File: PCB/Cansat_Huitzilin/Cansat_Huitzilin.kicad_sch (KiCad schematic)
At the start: 0 parts

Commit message: Actualización de la PCB
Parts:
- added C1: 10uf, Capacitor_SMD:C_0603_1608Metric, symbol Device:C
- added C10, C11, C12, C9: 22uF, Capacitor_SMD:C_0603_1608Metric, symbol Device:C
- added C13, C14, C2: 10uF, Capacitor_SMD:C_0603_1608Metric, symbol Device:C
- added C15, C17, C18, C19, C20, C22, C23, C3, C5, C8: 100nF, Capacitor_SMD:C_0603_1608Metric, symbol Device:C
- added C16: 1uF, Capacitor_SMD:C_0603_1608Metric, symbol Device:C
- added C21: 2.2uF, Capacitor_SMD:C_0603_1608Metric, symbol Device:C
- added C25, C26: C_Polarized, Capacitor_SMD:CP_Elec_6.3x5.8, symbol Device:C_Polarized
- added C4, C7: 10nF, Capacitor_SMD:C_0603_1608Metric, symbol Device:C
- added C6: 2.7nF, Capacitor_SMD:C_0603_1608Metric, symbol Device:C
- added D1: D_Schottky, Diode_SMD:D_SOD-123F, symbol Device:D_Schottky
- added H1, H2, H3, H4: MountingHole_Pad, MountingHole:MountingHole_3.2mm_M3, symbol Mechanical:MountingHole_Pad
- added IC1: AP64501SP-13, Package_SO:SOIC-8-1EP_3.9x4.9mm_P1.27mm_EP2.29x3mm, symbol AP64501SP-13:AP64501SP-13
- added IC2: 114993390, 114993390, symbol SamacSys_Parts:114993390
- added IC3: BMM350, BGA9C40P3X3_128X128X54, symbol SamacSys_Parts:BMM350
- added IC4: BMI323, BMI323, symbol SamacSys_Parts:BMI323
- added IC5: STCC4-D-R3, STCC4DR3, symbol SamacSys_Parts:STCC4-D-R3
- added IC6: SHT40-AD1B-R2, SHT40AD1BR2, symbol SamacSys_Parts:SHT40-AD1B-R2
- added J1: Screw_Terminal_01x02, TerminalBlock:TerminalBlock_MaiXu_MX126-5.0-02P_1x02_P5.00mm, symbol Connector:Screw_Terminal_01x02
- added J2: Conn_01x04, Connector_PinHeader_2.54mm:PinHeader_1x04_P2.54mm_Vertical, symbol Connector_Generic:Conn_01x04
- added J3, J5: Conn_01x03, Connector_PinHeader_2.54mm:PinHeader_1x03_P2.54mm_Vertical, symbol Connector_Generic:Conn_01x03
- added J4: Conn_01x06, SM06BPASSTBTLFSN, symbol Connector_Generic:Conn_01x06
- added J6: 503398-1892, 5033981892, symbol SamacSys_Parts:503398-1892
- added L1: 3.3uH, Inductor_SMD:L_Wuerth_WE-PD-Typ-LS, symbol Device:L_Ferrite
- added L2: 10uH, Inductor_SMD:L_1210_3225Metric_Pad1.42x2.65mm_HandSolder, symbol Device:L_Ferrite
- added LS1: MLT-8530, MLT8530, symbol SamacSys_Parts:MLT-8530
- added PS1: LD39200DPUR, SON80P400X400X100-9N-D, symbol SamacSys_Parts:LD39200DPUR
- added Q1: NPN, Package_TO_SOT_SMD:SOT-23, symbol Simulation_SPICE:NPN
- added R1: 100k, Resistor_SMD:R_0603_1608Metric, symbol Device:R_US
- added R10, R12, R13, R14, R15, R16, R17, R5, R9: 10k, Resistor_SMD:R_0603_1608Metric, symbol Device:R_US
- added R11: 1k, Resistor_SMD:R_0603_1608Metric, symbol Device:R_US
- added R2: 15.8k, Resistor_SMD:R_0603_1608Metric, symbol Device:R_US
- added R3: 2.2k, Resistor_SMD:R_0603_1608Metric, symbol Device:R_US
- added R4: 8.87k, Resistor_SMD:R_0603_1608Metric, symbol Device:R_US
- added R6, R7: 4.7k, Resistor_SMD:R_0603_1608Metric, symbol Device:R_US
- added R8: 56k, Resistor_SMD:R_0603_1608Metric, symbol Device:R_US
- added S1, S2: PTS526SM15SMTR2_LFS, PTS526SM15SMTR2LFS, symbol SamacSys_Parts:PTS526SM15SMTR2_LFS
- added SW1: SW_Wuerth_450301014042, Button_Switch_THT:SW_Slide-03_Wuerth-WS-SLTV_10x2.5x6.4_P2.54mm, symbol Switch:SW_Wuerth_450301014042
- added TP1, TP2: TestPoint, TestPoint:TestPoint_Pad_D1.0mm, symbol Connector:TestPoint
- added U1: ESP32-S3-MINI-1U, RF_Module:ESP32-S2-MINI-1U, symbol RF_Module:ESP32-S3-MINI-1U
- added U3: BMP581, BMP581, symbol SamacSys_Parts:BMP581
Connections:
- new net: J6.8 (DAT1), R16.1
- new net: IC1.3 (EN), R1.2, TP1.1
- new net: C10.1, C11.1, C7.2, C8.1, C9.1, L1.2, L2.1, R4.1
- new net: PS1.3 (ADJ/SENSE), R8.1, R9.2
- new net: PS1.5 (PG), TP2.1
- new net: C4.1, IC1.4 (SS)
- new net: D1.2 (A), LS1.3 (-LEAD), Q1.1 (C)
- new net: C5.1, IC1.1 (BST)
- new net: C7.1, IC1.5 (FB), R3.2, R4.2
- new net: IC1.6 (COMP), R2.2
- new net: C5.2, IC1.8 (SW), L1.1
- new net: C6.1, R2.1
- new net: J6.1 (DAT2), R17.1
- new net: Q1.2 (B), R11.2
- new net: C21.1, IC3.C2 (CRST)
- new net: IC5.2 (SDA_C), IC6.1 (SDA)
- new net +3.3V: C14.1, C15.1, C17.1, C18.1, C19.1, C20.1, C22.2, C23.1, IC2.8 (VCC), IC3.B3 (VDDIO), IC3.C1 (VDD), IC4.12 (CSB), IC4.5 (VDDIO), IC4.8 (VDD), IC5.6 (VDDIO), IC5.7 (VDD), IC6.3 (VDD), J2.4 (Pin_4), J6.4 (VDD), PS1.1 (OUT_1), PS1.2 (OUT_2), R10.2, R12.1, R13.2, R14.2, R15.2, R16.2, R17.2, R5.2, R6.1, R7.1, R8.2, U1.3 (3V3), U3.1 (VDDIO), U3.10 (VDD), U3.6 (CSB)
- new net +4V: C12.1, C13.1, C25.1, C26.1, D1.1 (K), J3.2 (Pin_2), J4.3 (Pin_3), J5.2 (Pin_2), L2.2, LS1.2 (+LEAD), PS1.6 (EN), PS1.7 (IN_1), PS1.8 (IN_2)
- new net +9V: J1.1 (Pin_1), SW1.1 (B)
- new net BOOT: R12.2, S2.1 (COM_1), U1.4 (IO0)
- new net BUSY: IC2.11 (BUSY), U1.13 (IO9)
- new net BUZZER: R11.1, U1.38 (IO42)
- new net CS_SD: J6.2 (CD/DAT3), R10.1, U1.37 (IO41)
- new net DIO1: IC2.12 (DIO1), U1.18 (IO14)
- new net Enable ESP: C16.1, R5.1, S1.1 (COM_1), U1.45 (EN)
- new net GND: C1.2, C10.2, C11.2, C12.2, C13.2, C14.2, C15.2, C16.2, C17.2, C18.2, C19.2, C2.2, C20.2, C21.2, C22.1, C23.2, C25.2, C26.2, C3.2, C4.2, C6.2, C8.2, C9.2, H1.1, H2.1, H3.1, H4.1, IC1.7 (GND), IC1.9 (EP), IC2.10 (GND_2), IC2.7 (GND_1), IC3.B1 (GND), IC3.B2 (ADSEL), IC3.C3 (BYPASS), IC4.1 (SDO), IC4.6 (GNDIO), IC4.7 (GND), IC5.3 (ADDR), IC5.4 (VSS), IC6.4 (VSS), J1.2 (Pin_2), J2.1 (Pin_1), J3.1 (Pin_1), J4.4 (Pin_4), J5.1 (Pin_1), J6.11, J6.12, J6.13, J6.14, J6.6 (VSS), PS1.4 (GND_1), PS1.9 (GND_2), Q1.3 (E), R3.1, R9.1, S1.3 (NO_1), S2.3 (NO_1), U1.1 (GND), U1.2 (GND), U1.42 (GND), U1.43 (GND), U1.46 (GND), U1.47 (GND), U1.48 (GND), U1.49 (GND), U1.50 (GND), U1.51 (GND), U1.52 (GND), U1.53 (GND), U1.54 (GND), U1.55 (GND), U1.56 (GND), U1.57 (GND), U1.58 (GND), U1.59 (GND), U1.60 (GND), U1.61 (GND), U1.62 (GND), U1.63 (GND), U1.64 (GND), U1.65 (GND), U3.3 (VSS_1), U3.5 (SDO), U3.8 (VSS_2), U3.9 (VSS_3)
- new net MISO: IC2.2 (MISO), J6.7 (DAT0), R15.1, U1.17 (IO13)
- new net MOSI: IC2.3 (MOSI), J6.3 (CMD), R13.1, U1.15 (IO11)
- new net NRST: IC2.5 (NRST), U1.25 (IO21)
- new net NSS: IC2.6 (NSS), U1.14 (IO10)
- new net RF_SW: IC2.1 (RF_SW_), U1.36 (IO40)
- new net RX: J2.2 (Pin_2), U1.40 (RXD0)
- new net RX_GPS: J4.5 (Pin_5), U1.21 (IO17)
- new net SCK: IC2.4 (SCK), J6.5 (CLK), R14.1, U1.16 (IO12)
- new net SCL: IC3.A3 (SCK), IC4.13 (SCX), IC5.1 (SCL), R7.2, U1.6 (IO2), U3.2 (SCK)
- new net SCL_SHT4: IC5.8 (SCL_C), IC6.2 (SCL)
- new net SDA: IC3.A2 (SDA), IC4.14 (SDX), IC5.5 (SDA), R6.2, U1.5 (IO1), U3.4 (SDI)
- new net SERVO 1: J3.3 (Pin_3), U1.8 (IO4)
- new net SERVO 2: J5.3 (Pin_3), U1.9 (IO5)
- new net Sw_9v: C1.1, C2.1, C3.1, IC1.2 (VIN), R1.1, SW1.3 (A)
- new net TX: J2.3 (Pin_3), U1.39 (TXD0)
- new net TX_GPS: J4.6 (Pin_6), U1.22 (IO18)
- no-connect marks 0 -> 20
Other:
- note added: "BMI-323"
- note added: "BMP-581"
- note added: "Buzzer"
- note added: "COMUNICACION"
- note added: "Conector"
- note added: "DC-DC BUCK 4V OUT"
- note added: "Enable ESP32"
- note added: "GPS UART"
- note added: "I2C BUS"
- note added: "LECTOR SD"
- note added: "LIS2MDL"
- note added: "PROGRAMACION POR UART"
- note added: "Regulador Lineal 4v a 3.3v"
- note added: "SERVOS"
- note added: "STCC4"
- note added: "SWITCH 9V"
- company: (none) -> S.T.R.I.K.E.
- title: (none) -> Cansat

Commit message: Actualización del diseño PCB
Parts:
- added J7: Conn_01x04, Connector_PinHeader_2.54mm:PinHeader_1x04_P2.54mm_Vertical, symbol Connector_Generic:Conn_01x04
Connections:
- net +3.3V: now also J7.4 (Pin_4)
- net GND: now also J7.1 (Pin_1)
- net TX_PI: now reaches U1.27 (IO47)
- net TX_PI: now also J7.3 (Pin_3)
- net RX_PI: now reaches U1.30 (IO48)
- net RX_PI: now also J7.2 (Pin_2)
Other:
- note added: "pi"

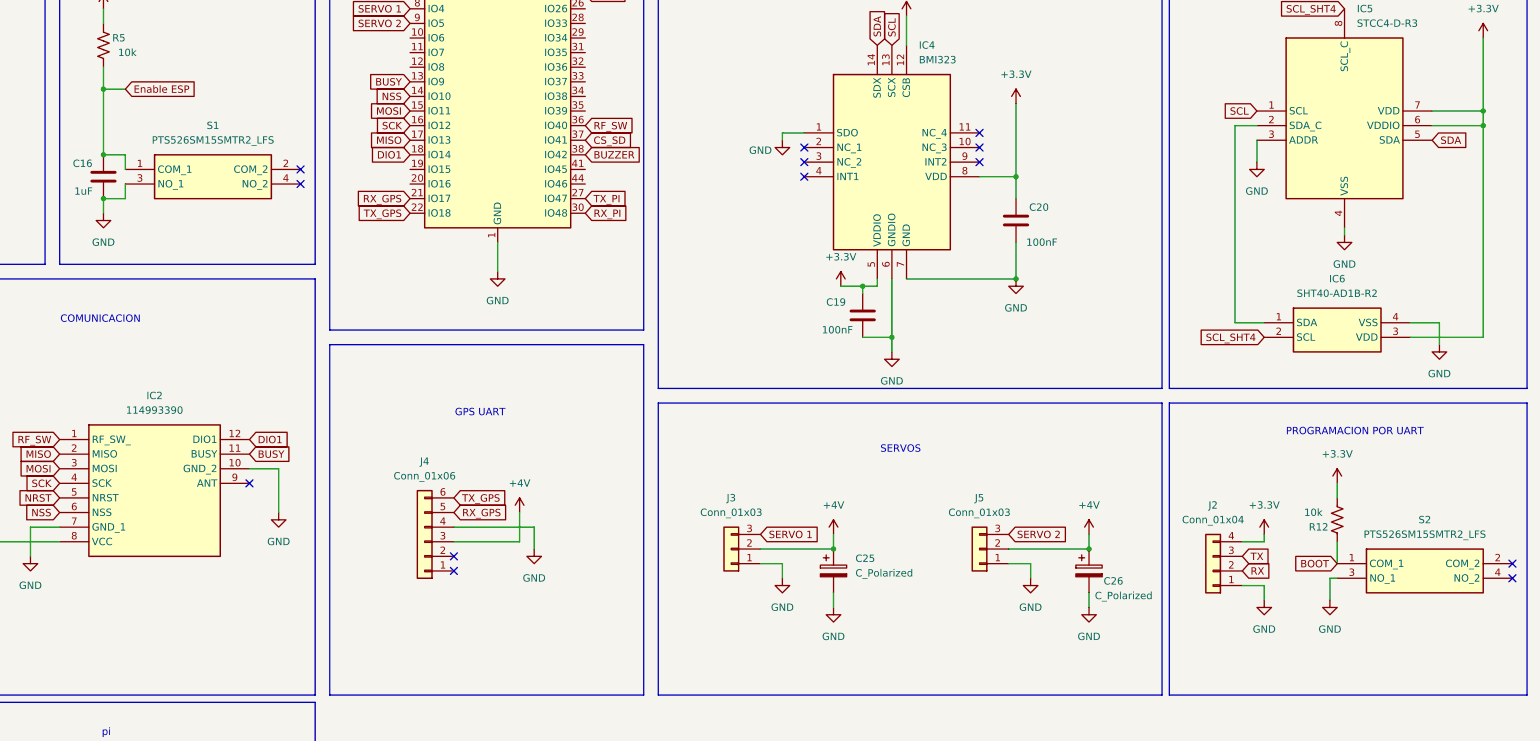
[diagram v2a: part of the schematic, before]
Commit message: PCB
adding the final serigraphy
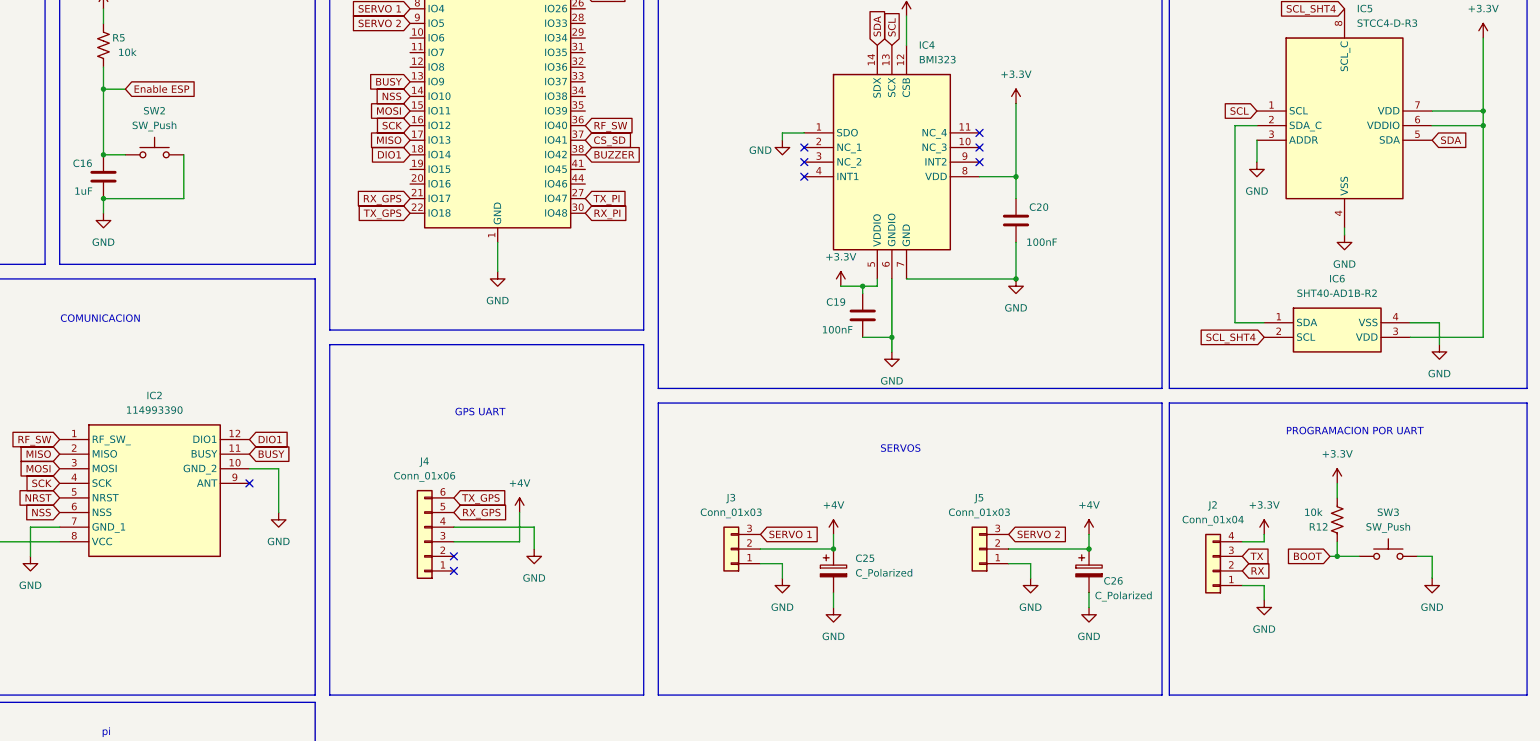
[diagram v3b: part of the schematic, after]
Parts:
- removed S1, S2: PTS526SM15SMTR2_LFS, PTS526SM15SMTR2LFS, symbol SamacSys_Parts:PTS526SM15SMTR2_LFS
- added SW2, SW3: SW_Push, Button_Switch_SMD:SW_SPST_SKQG_WithoutStem, symbol Switch:SW_Push
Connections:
- net BOOT: now also SW3.1
- net Enable ESP: now also SW2.1
- net GND: now also SW2.2, SW3.2
- no-connect marks 20 -> 16
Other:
- company: S.T.R.I.K.E. -> S.T.R.I.K.E. Aerospace
- title: Cansat -> SCH_Cansat-Huitzilin

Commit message: GUI & PCB
Complete Mission Control v1.0.1 and integrate final CanSat PCB + libraries
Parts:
- IC2: footprint 114993390 -> SamacSys_Parts:114993390
- IC3: footprint BGA9C40P3X3_128X128X54 -> SamacSys_Parts:BGA9C40P3X3_128X128X54
- IC4: footprint BMI323 -> SamacSys_Parts:BMI323
- IC5: footprint STCC4DR3 -> SamacSys_Parts:STCC4DR3
- IC6: footprint SHT40AD1BR2 -> SamacSys_Parts:SHT40AD1BR2
- J4: footprint SM06BPASSTBTLFSN -> SamacSys_Parts:SM06BPASSTBTLFSN
- J6: footprint 5033981892 -> SamacSys_Parts:5033981892
- LS1: footprint MLT8530 -> SamacSys_Parts:MLT8530
- PS1: footprint SON80P400X400X100-9N-D -> SamacSys_Parts:SON80P400X400X100-9N-D
- U3: footprint BMP581 -> SamacSys_Parts:BMP581
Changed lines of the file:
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@@
 			)
 		)
-		(property "Footprint" "BMI323"
+		(property "Footprint" "SamacSys_Parts:BMI323"
 			(at 308.61 207.95 0)
 			(effects
@@
 			)
 		)
-		(property "Footprint" "SON80P400X400X100-9N-D"
+		(property "Footprint" "SamacSys_Parts:SON80P400X400X100-9N-D"
 			(at 93.98 199.06 0)
 			(effects
@@
 			)
 		)
-		(property "Footprint" "MLT8530"
+		(property "Footprint" "SamacSys_Parts:MLT8530"
 			(at 105.41 336.22 0)
 			(effects
@@
 			)
 		)
-		(property "Footprint" "SM06BPASSTBTLFSN"
+		(property "Footprint" "SamacSys_Parts:SM06BPASSTBTLFSN"
 			(at 215.9 191.77 0)
 			(effects
@@
 			)
 		)
-		(property "Footprint" "BGA9C40P3X3_128X128X54"
+		(property "Footprint" "SamacSys_Parts:BGA9C40P3X3_128X128X54"
 			(at 381 135.56 0)
 			(effects
@@
 			)
 		)
-		(property "Footprint" "SHT40AD1BR2"
+		(property "Footprint" "SamacSys_Parts:SHT40AD1BR2"
 			(at 383.54 248.59 0)
 			(effects
@@
 			)
 		)
-		(property "Footprint" "STCC4DR3"
+		(property "Footprint" "SamacSys_Parts:STCC4DR3"
 			(at 387.35 201.6 0)
 			(effects
@@
 			)
 		)
-		(property "Footprint" "114993390"
+		(property "Footprint" "SamacSys_Parts:114993390"
 			(at 181.61 268.91 0)
 			(effects
@@
 			)
 		)
-		(property "Footprint" "BMP581"
+		(property "Footprint" "SamacSys_Parts:BMP581"
 			(at 312.42 133.02 0)
 			(effects
@@
 			)
 		)
-		(property "Footprint" "5033981892"
+		(property "Footprint" "SamacSys_Parts:5033981892"
 			(at 109.22 290.5 0)
 			(effects

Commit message: save
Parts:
- removed IC5: STCC4-D-R3, SamacSys_Parts:STCC4DR3, symbol SamacSys_Parts:STCC4-D-R3
- removed IC6: SHT40-AD1B-R2, SamacSys_Parts:SHT40AD1BR2, symbol SamacSys_Parts:SHT40-AD1B-R2
- H1, H2, H3, H4: footprint MountingHole:MountingHole_3.2mm_M3 -> MountingHole:MountingHole_3.2mm_M3_Pad_Via
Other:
- note removed: "STCC4"
